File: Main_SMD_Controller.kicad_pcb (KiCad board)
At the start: 2 copper layers, 65 x 85 mm, 49 parts, among them J1 2.1-5.5 +12VDC, J10 Vin_-, J11 Conn_01x02, J12 Vsens, J13 Vin+, J2 Switch_Control, J3 +5V, J4 AnalogIO, J5 +12V, J6 VsensJMP, J7 Drain, J8 Gate, J9 Source, P1 Eoshi-chan_Silk, P2 Eoshi-chan_Silk, P3 Serial_QR, Q1 2N7002K, U1 NJM7805SDL1, U2 TC74HC4066AF(F), U3 AD8226ARZ, U4 S-89713B-K8T2U

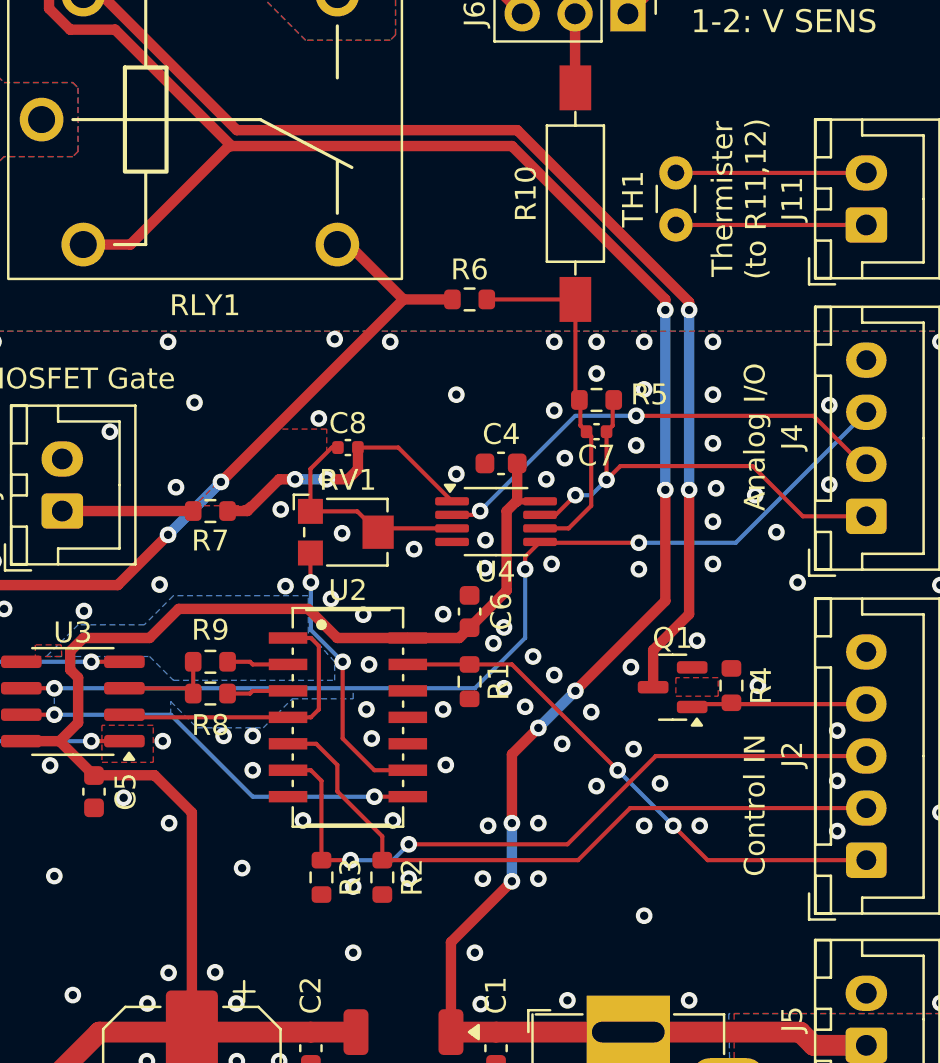
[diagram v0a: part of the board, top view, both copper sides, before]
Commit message: add BOM
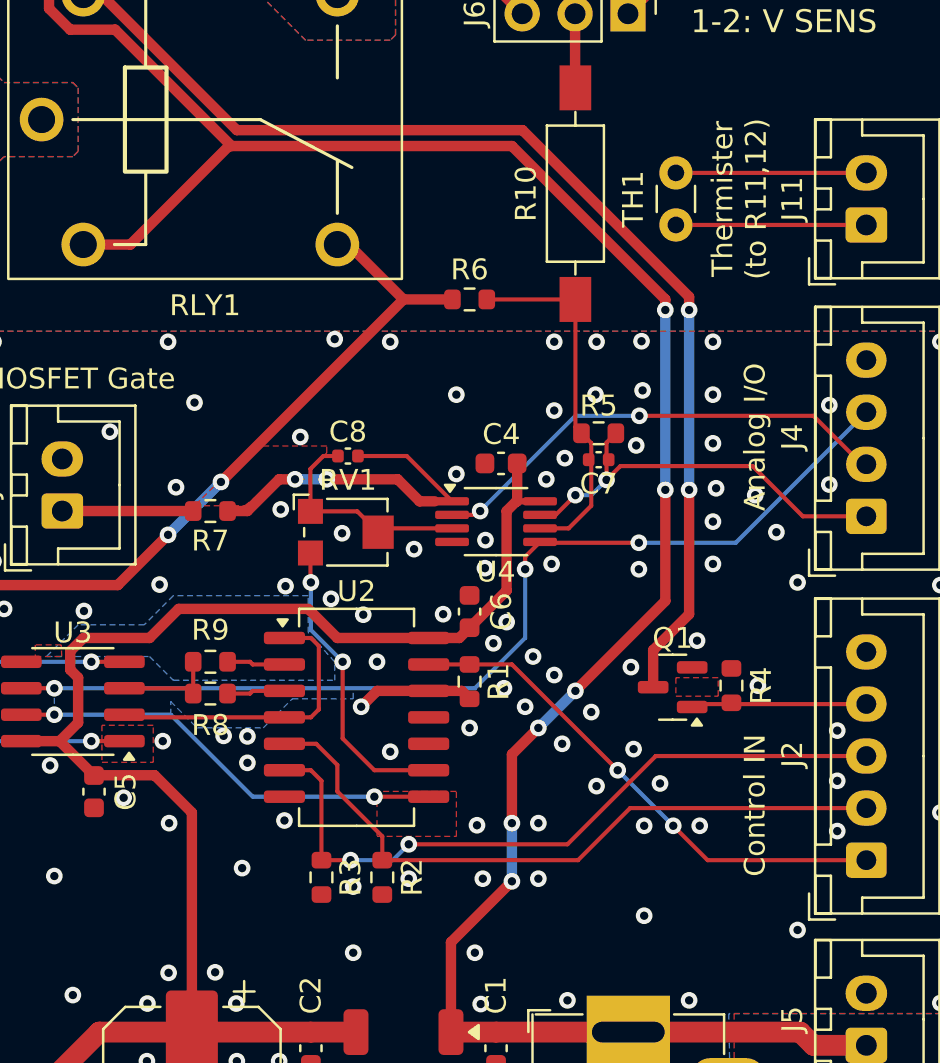
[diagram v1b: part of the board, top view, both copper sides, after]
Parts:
- U2: footprint Package_DMP:DMP-14_10x5_P1.27mm -> Package_SO:SO-14_5.3x10.2mm_P1.27mm
- moved R5 1.60 mm to (77.3, 72.2)
- moved C7 1.35 mm to (77.3, 73.5)
- moved U2 0.41 mm to (65.7, 85.9), turned to 0 degrees
- moved C8 0.41 mm to (65.3, 73.3)
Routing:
- net GND: track 0.00 -> 5.68 mm, vias 118 -> 117
- net Net-(C8-Pad2): track 13.7 -> 17.3 mm
- net /Vmeas: track 21.6 -> 20.1 mm
- net SHUNT_SELECT2: track 25.9 -> 24.9 mm
- net Net-(U2-Pad8): track 20.2 -> 21.2 mm
- net Net-(RV1-Pad3): track 13.3 -> 14.3 mm

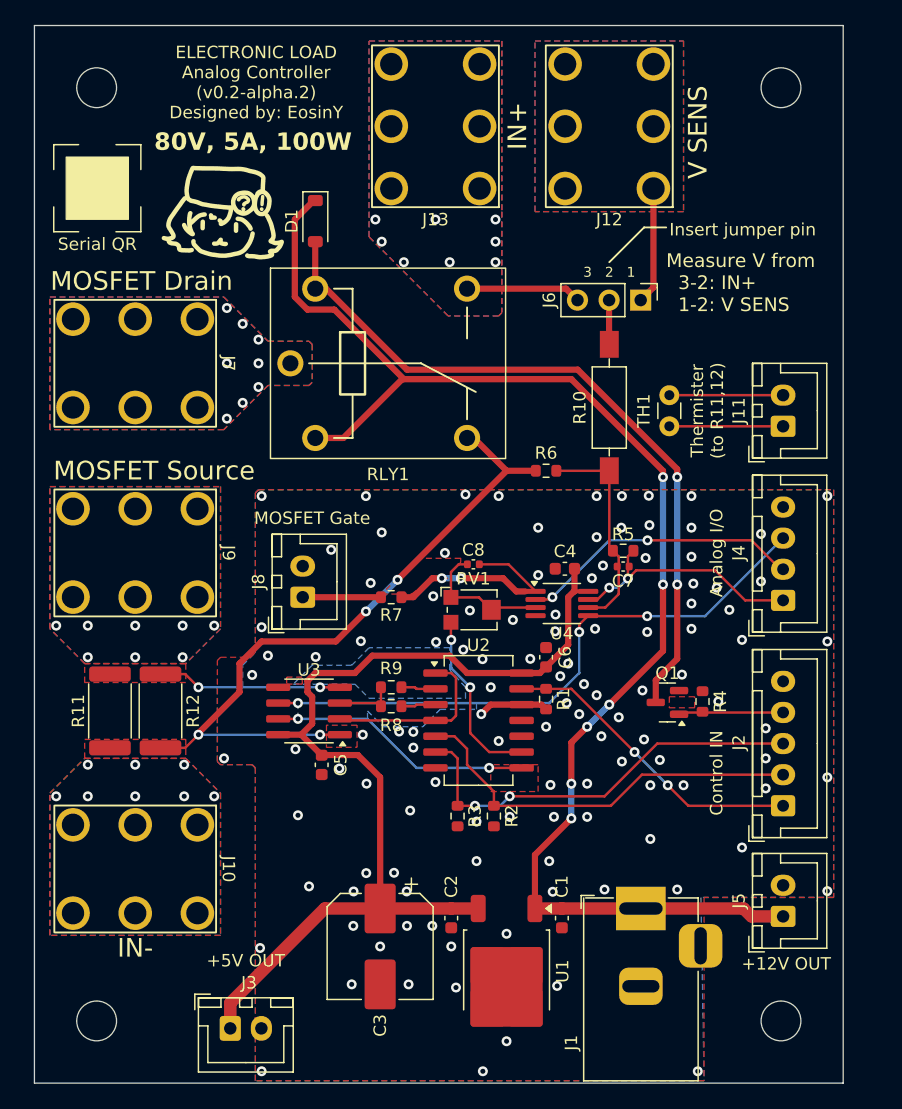
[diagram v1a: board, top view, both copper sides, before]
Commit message: changed library
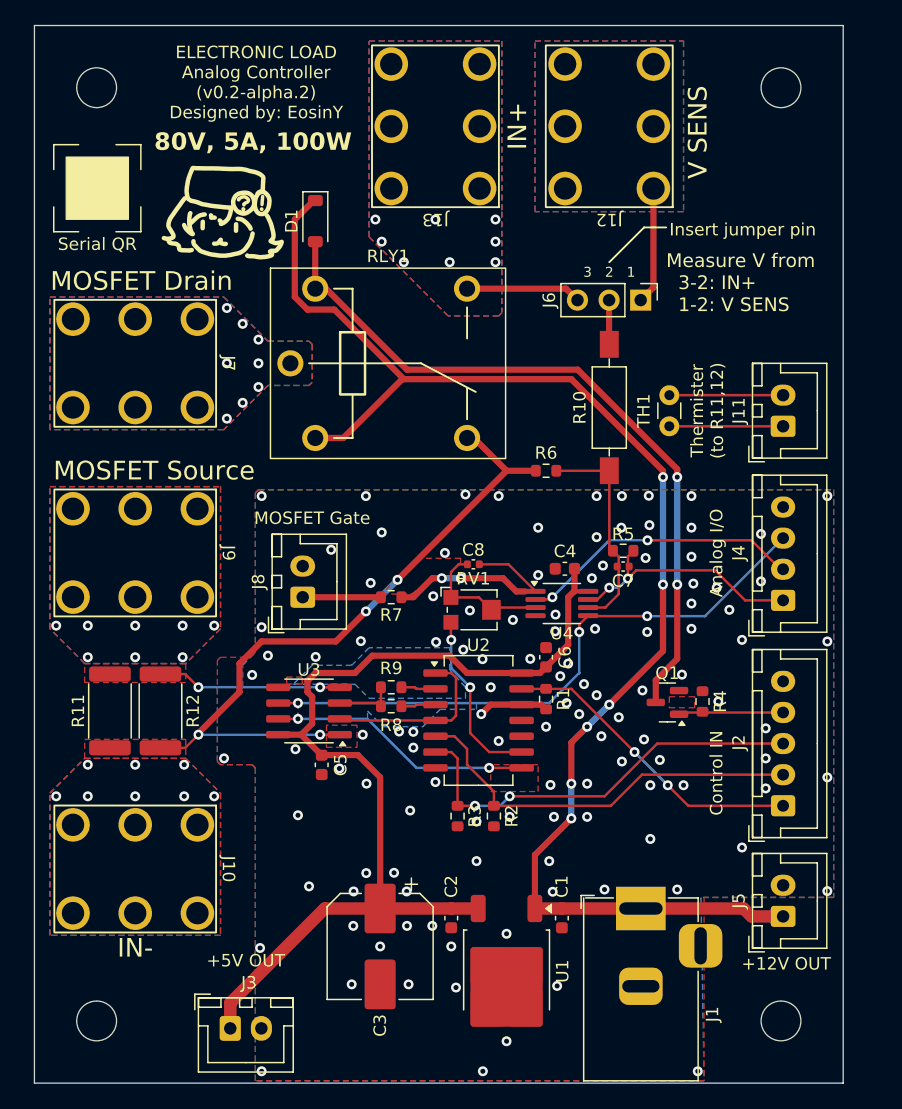
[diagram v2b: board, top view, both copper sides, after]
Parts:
- J1: footprint Akizuki_BarrelJack:BarrelJack_Horizontal1 -> AM_Conn_BarrelJack:MJ-179P(H)
- J10, J12, J13, J7, J9: footprint Akizuki_ScrewTerminal:ScrewTerminal_01x01_PCB-20 -> AM_Conn_ScrewTerminal:ScrewTerminal_01x01_PCB-20
- RLY1: footprint Akizuki_Relay:HSINDA-943_12A-1C_5p -> AM_Relay:HSINDA-943_12A-1C_5p
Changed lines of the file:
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@@
 		(sheetname "/")
 		(sheetfile "Main_SMD_Controller.kicad_sch")
-		(attr exclude_from_pos_files)
+		(attr exclude_from_pos_files exclude_from_bom)
 		(fp_circle
 			(center 0 0)
@@
 		)
 	)
-	(footprint "Akizuki_BarrelJack:BarrelJack_Horizontal1"
+	(footprint "AM_Conn_BarrelJack:MJ-179P(H)"
 		(layer "F.Cu")
 		(at 78.74 114.715 90)
@@
 		(tags "Power Jack")
 		(property "Reference" "J1"
-			(at 2.955 -5.588 90)
+			(at 5.25 5.75 90)
 			(layer "F.SilkS")
 			(effects
@@
 		)
 		(embedded_fonts no)
-		(model "C:/Users/EosinY/Documents/KiCad/Footprints/Akizuki/BarrelJack/BarrelJack_Horizontal1.STEP"
+		(model "C:/Users/EosinY/Documents/KiCad/Footprints/3dmodel/AM/Conn/BarrelJack/BarrelJack_Horizontal1.STEP"
 			(offset
 				(xyz 7.25 0 0)
@@
 		)
 	)
-	(footprint "Akizuki_Relay:HSINDA-943_12A-1C_5p"
+	(footprint "AM_Relay:HSINDA-943_12A-1C_5p"
 		(layer "F.Cu")
 		(at 58.42 57.15)
+		(descr "943-1C-xxDS")
+		(tags "Relay")
 		(property "Reference" "RLY1"
-			(at 0 8.926 0)
+			(at 0 -8.6 0)
 			(unlocked yes)
 			(layer "F.SilkS")
@@
 			)
 		)
-		(property "Category" "Relays"
+		(property "Digi-Key_PN" "Z1011-ND"
 			(at 0 0 0)
+			(unlocked yes)
 			(layer "F.Fab")
 			(hide yes)
@@
 			)
 		)
-		(property "DK_Datasheet_Link" "https://omronfs.omron.com/en_US/ecb/products/pdf/en-g5le.pdf"
+		(property "MPN" "G5LE-14 DC5"
 			(at 0 0 0)
+			(unlocked yes)
 			(layer "F.Fab")
 			(hide yes)
@@
 			)
 		)
-		(property "DK_Detail_Page" "/product-detail/en/omron-electronics-inc-emc-div/G5LE-14-DC5/Z1011-ND/280371"
+		(property "Category" "Relays"
 			(at 0 0 0)
+			(unlocked yes)
 			(layer "F.Fab")
 			(hide yes)
@@
 			)
 		)
-		(property "Digi-Key_PN" "Z1011-ND"
+		(property "Family" "Power Relays, Over 2 Amps"
 			(at 0 0 0)
+			(unlocked yes)
 			(layer "F.Fab")
 			(hide yes)
@@
 			)
 		)
-		(property "Family" "Power Relays, Over 2 Amps"
+		(property "DK_Datasheet_Link" "https://omronfs.omron.com/en_US/ecb/products/pdf/en-g5le.pdf"
 			(at 0 0 0)
+			(unlocked yes)
 			(layer "F.Fab")
 			(hide yes)
@@
 			)
 		)
-		(property "MPN" "G5LE-14 DC5"
+		(property "DK_Detail_Page" "/product-detail/en/omron-electronics-inc-emc-div/G5LE-14-DC5/Z1011-ND/280371"
 			(at 0 0 0)
+			(unlocked yes)
 			(layer "F.Fab")
 			(hide yes)
@@
 		(property "Manufacturer" "Omron Electronics Inc-EMC Div"
 			(at 0 0 0)
+			(unlocked yes)
 			(layer "F.Fab")
 			(hide yes)
@@
 		(property "Status" "Active"
 			(at 0 0 0)
+			(unlocked yes)
 			(layer "F.Fab")
 			(hide yes)
@@
 		)
 		(embedded_fonts no)
-		(model "C:/Users/EosinY/Documents/KiCad/Footprints/Akizuki/Relay/943-1C-12DS.STEP"
+		(model "C:/Users/EosinY/Documents/KiCad/Footprints/3dmodel/AM/Relay/943-1C-12DS.STEP"
 			(offset
 				(xyz 0 0 0)
@@
 		)
 	)
-	(footprint "Akizuki_ScrewTerminal:ScrewTerminal_01x01_PCB-20"
+	(footprint "AM_Conn_ScrewTerminal:ScrewTerminal_01x01_PCB-20"
 		(layer "F.Cu")
 		(at 38.1 97.79 -90)
+		(descr "PCB-20 (Code: x1: 112148, x10: 105115)")
+		(tags "Screw terminal")
 		(property "Reference" "J10"
 			(at 0 -7.5 270)
@@
 		(sheetname "/")
 		(sheetfile "Main_SMD_Controller.kicad_sch")
-		(attr board_only exclude_from_pos_files)
+		(attr board_only exclude_from_pos_files exclude_from_bom)
 		(fp_poly
 			(pts
@@
 		(sheetname "/")
 		(sheetfile "Main_SMD_Controller.kicad_sch")
-		(attr exclude_from_pos_files)
+		(attr exclude_from_pos_files exclude_from_bom)
 		(fp_circle
 			(center 0 0)
@@
 		(embedded_fonts no)
 	)
-	(footprint "Akizuki_ScrewTerminal:ScrewTerminal_01x01_PCB-20"
+	(footprint "AM_Conn_ScrewTerminal:ScrewTerminal_01x01_PCB-20"
 		(layer "F.Cu")
 		(at 38.1 57.15 -90)
+		(descr "PCB-20 (Code: x1: 112148, x10: 105115)")
+		(tags "Screw terminal")
 		(property "Reference" "J7"
 			(at 0 -7.5 270)
@@
 		(embedded_fonts no)
 	)
-	(footprint "Akizuki_ScrewTerminal:ScrewTerminal_01x01_PCB-20"
+	(footprint "AM_Conn_ScrewTerminal:ScrewTerminal_01x01_PCB-20"
 		(layer "F.Cu")
 		(at 38.1 72.39 -90)
+		(descr "PCB-20 (Code: x1: 112148, x10: 105115)")
+		(tags "Screw terminal")
 		(property "Reference" "J9"
 			(at 0 -7.5 270)
@@
 		(sheetname "/")
 		(sheetfile "Main_SMD_Controller.kicad_sch")
+		(attr exclude_from_bom)
 		(fp_line
 			(start -3.5 -3.5)
@@
 		(sheetname "/")
 		(sheetfile "Main_SMD_Controller.kicad_sch")
-		(attr exclude_from_pos_files)
+		(attr exclude_from_pos_files exclude_from_bom)
 		(fp_circle
 			(center 0 0)
@@
 		(sheetname "/")
 		(sheetfile "Main_SMD_Controller.kicad_sch")
-		(attr exclude_from_pos_files)
+		(attr exclude_from_pos_files exclude_from_bom)
 		(fp_circle
 			(center 0 0)
@@
 		)
 	)
-	(footprint "Akizuki_ScrewTerminal:ScrewTerminal_01x01_PCB-20"
+	(footprint "AM_Conn_ScrewTerminal:ScrewTerminal_01x01_PCB-20"
 		(layer "F.Cu")
 		(at 62.23 38.1 180)
+		(descr "PCB-20 (Code: x1: 112148, x10: 105115)")
+		(tags "Screw terminal")
 		(property "Reference" "J13"
-			(at 0 -7.5 0)
+			(at 0 -7.5 180)
 			(unlocked yes)
 			(layer "F.SilkS")
@@
 		(embedded_fonts no)
 	)
-	(footprint "Akizuki_ScrewTerminal:ScrewTerminal_01x01_PCB-20"
+	(footprint "AM_Conn_ScrewTerminal:ScrewTerminal_01x01_PCB-20"
 		(layer "F.Cu")
 		(at 76.2 38.1 180)
+		(descr "PCB-20 (Code: x1: 112148, x10: 105115)")
+		(tags "Screw terminal")
 		(property "Reference" "J12"
-			(at 0 -7.5 0)
+			(at 0 -7.5 180)
 			(unlocked yes)
 			(layer "F.SilkS")
@@
 		(sheetname "/")
 		(sheetfile "Main_SMD_Controller.kicad_sch")
-		(attr board_only exclude_from_pos_files)
+		(attr board_only exclude_from_pos_files exclude_from_bom)
 		(fp_poly
 			(pts
